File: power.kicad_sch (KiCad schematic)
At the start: 22 parts, among them U5 LM66100, U6 LM66100, U7 MAX77827AEFD+T, U8 SC4215

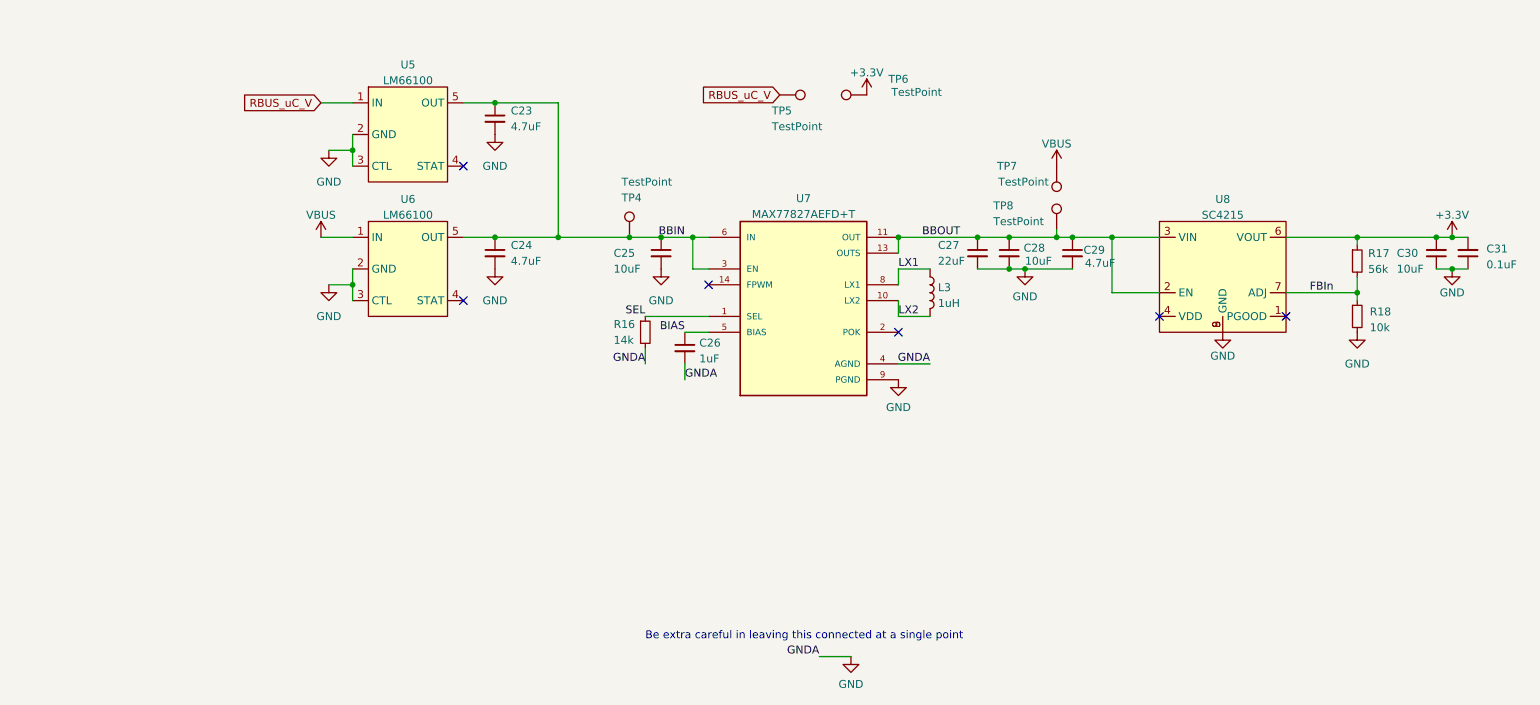
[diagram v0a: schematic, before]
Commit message: updated ideal oring diode and layout
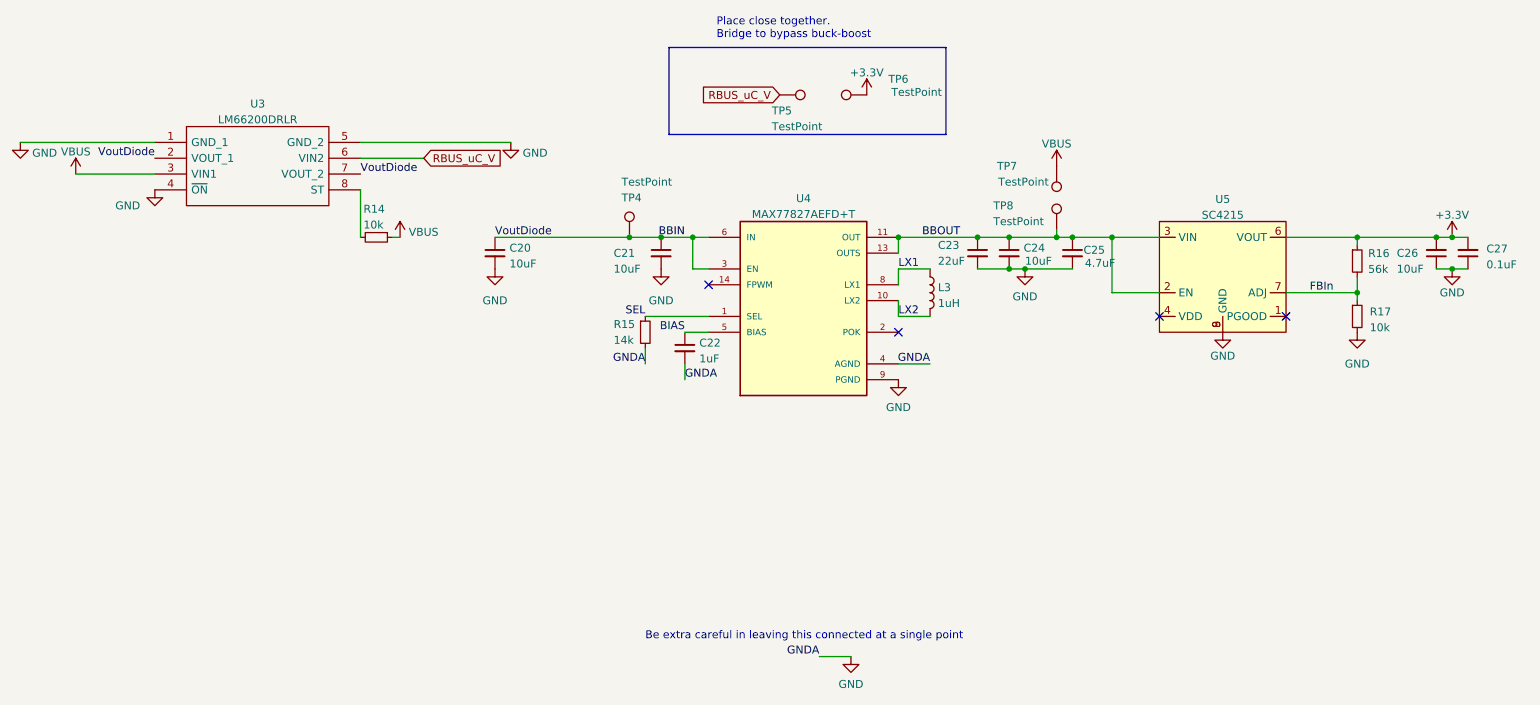
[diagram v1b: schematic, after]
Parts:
- removed C23: 4.7uF, Capacitor_SMD:C_0402_1005Metric, symbol Device:C_Small
- removed U5, U6: LM66100, Package_TO_SOT_SMD:SOT-23-5, symbol iclr:LTC4411
- added R14: 10k, Resistor_SMD:R_0402_1005Metric, symbol Device:R_Small
- added U3: LM66200DRLR, SOTFL50P160X60-8N, symbol iclr:LM66200DRLR
- C20: renamed from C24; value 4.7uF -> 10uF
- renumbered C25 to C21, C26 to C22, C27 to C23, C28 to C24, C29 to C25, C30 to C26, C31 to C27, R16 to R15, R17 to R16, R18 to R17, U7 to U4, U8 to U5
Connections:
- net BBIN: now also U3.2 (VOUT_1), U3.7 (VOUT_2)
- net GND: now also U3.1 (GND_1), U3.4 (~{ON}), U3.5 (GND_2)
- net RBUS_uC_V: now also U3.6 (VIN2)
- net VBUS: now also R14.1, U3.3 (VIN1)
- new net: R14.2, U3.8 (ST)
- no-connect marks 6 -> 4
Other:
- note added: "Place close together. Bridge to bypass buck-boost"

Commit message: changed usb port footprint to the combined SMD/THT one
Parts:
- U3: footprint SOTFL50P160X60-8N -> iclr:SOTFL50P160X60-8N
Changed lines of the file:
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@@
     (property "Reference" "U3" (id 0) (at 63.5 30.641 0))
     (property "Value" "LM66200DRLR" (id 1) (at 63.5 33.1779 0))
-    (property "Footprint" "SOTFL50P160X60-8N" (id 2) (at 76.2 34.29 0)
+    (property "Footprint" "iclr:SOTFL50P160X60-8N" (id 2) (at 76.2 34.29 0)
       (effects (font (size 1.27 1.27)) (justify left) hide)
     )

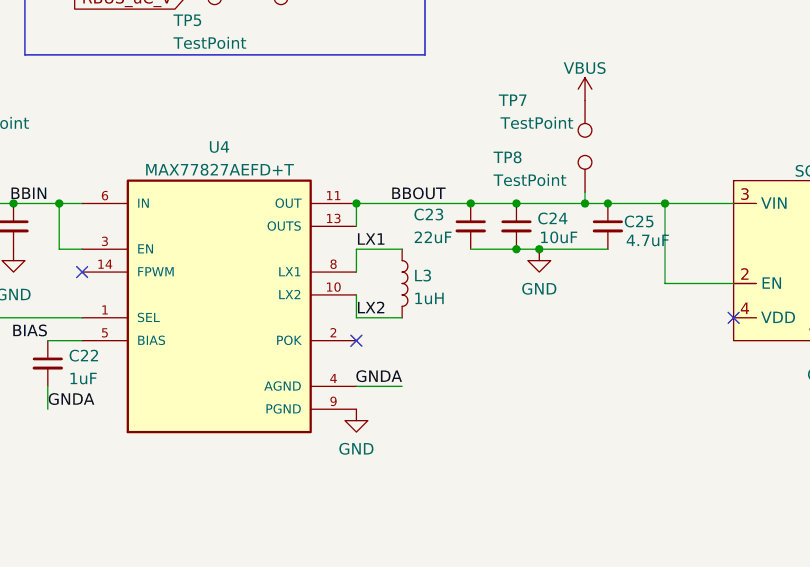
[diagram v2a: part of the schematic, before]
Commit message: updated some schematic values
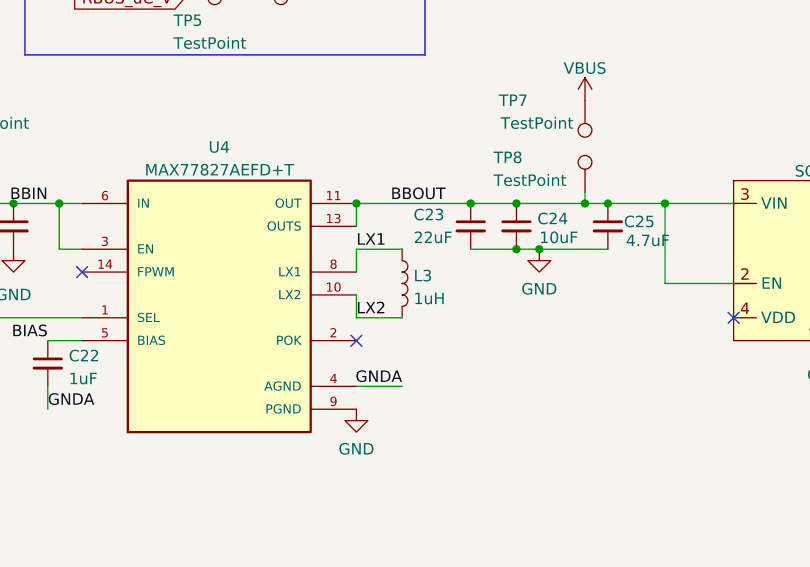
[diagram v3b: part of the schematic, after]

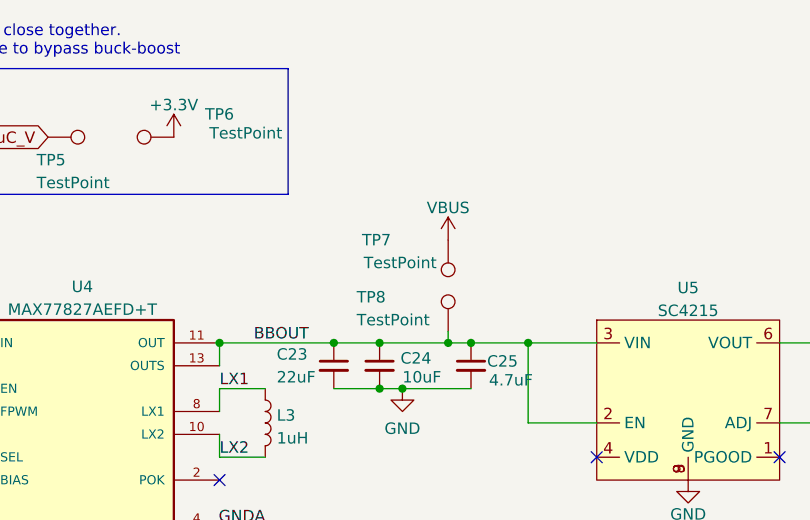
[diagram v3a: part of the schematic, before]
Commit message: implemented fixes that were changed for ordering of nimbus flight electronics, tidied up layout and set up manufacturing constraints
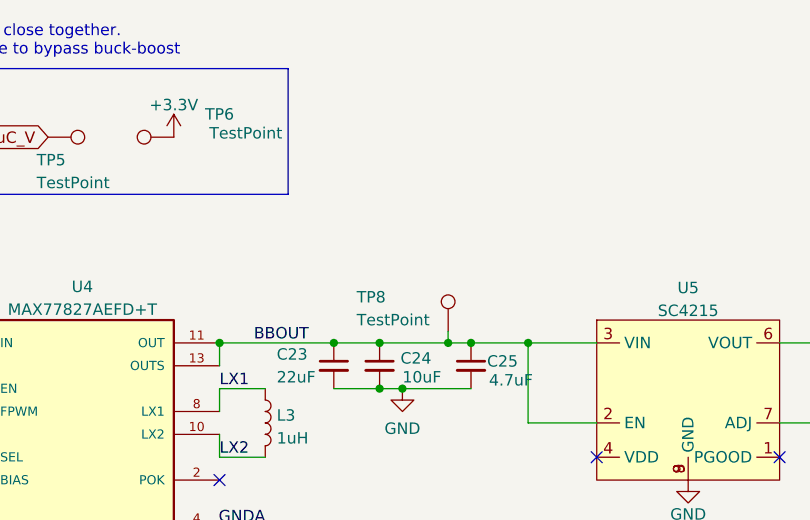
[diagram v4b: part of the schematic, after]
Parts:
- removed TP7: TestPoint, TestPoint:TestPoint_Pad_D1.5mm, symbol Connector:TestPoint
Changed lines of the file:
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@@
-    )
-  )
-  (symbol (lib_id "power:VBUS") (at 191.77 40.64 0) (unit 1)
-    (in_bom yes) (on_board yes) (dnp no) (fields_autoplaced)
-    (property "Reference" "#PWR046" (at 191.77 44.45 0)
-      (effects (font (size 1.27 1.27)) hide)
-    )
-    (property "Value" "VBUS" (at 191.77 37.0642 0)
-      (effects (font (size 1.27 1.27)))
-    )
-    (property "Footprint" "" (at 191.77 40.64 0)
-      (effects (font (size 1.27 1.27)) hide)
-    )
-    (property "Datasheet" "" (at 191.77 40.64 0)
-      (effects (font (size 1.27 1.27)) hide)
-    )
-    (pin "1")
-    (instances
-      (project "RicardoTemplate"
-        (path "/7db990e4-92e1-4f99-b4d2-435bbec1ba83/48a413b4-b7c2-44ac-971c-583c31b73475"
-          (reference "#PWR046") (unit 1)
-        )
-      )
     )
   )
@@
         )
       )
-    )
-  )
-  (symbol (lib_id "Connector:TestPoint") (at 191.77 40.64 180) (unit 1)
-    (in_bom yes) (on_board yes) (dnp no)
-    (property "Reference" "TP7" (at 185.42 40.64 0)
-      (effects (font (size 1.27 1.27)) (justify left))
-    )
-    (property "Value" "TestPoint" (at 190.5 43.1769 0)
-      (effects (font (size 1.27 1.27)) (justify left))
-    )
-    (property "Footprint" "TestPoint:TestPoint_Pad_D1.5mm" (at 186.69 40.64 0)
-      (effects (font (size 1.27 1.27)) hide)
-    )
-    (property "Datasheet" "~" (at 186.69 40.64 0)
-      (effects (font (size 1.27 1.27)) hide)
-    )
-    (pin "1")
-    (instances
-      (project "RicardoTemplate"
-        (path "/7db990e4-92e1-4f99-b4d2-435bbec1ba83/48a413b4-b7c2-44ac-971c-583c31b73475"
-          (reference "TP7") (unit 1)
-        )
-      )

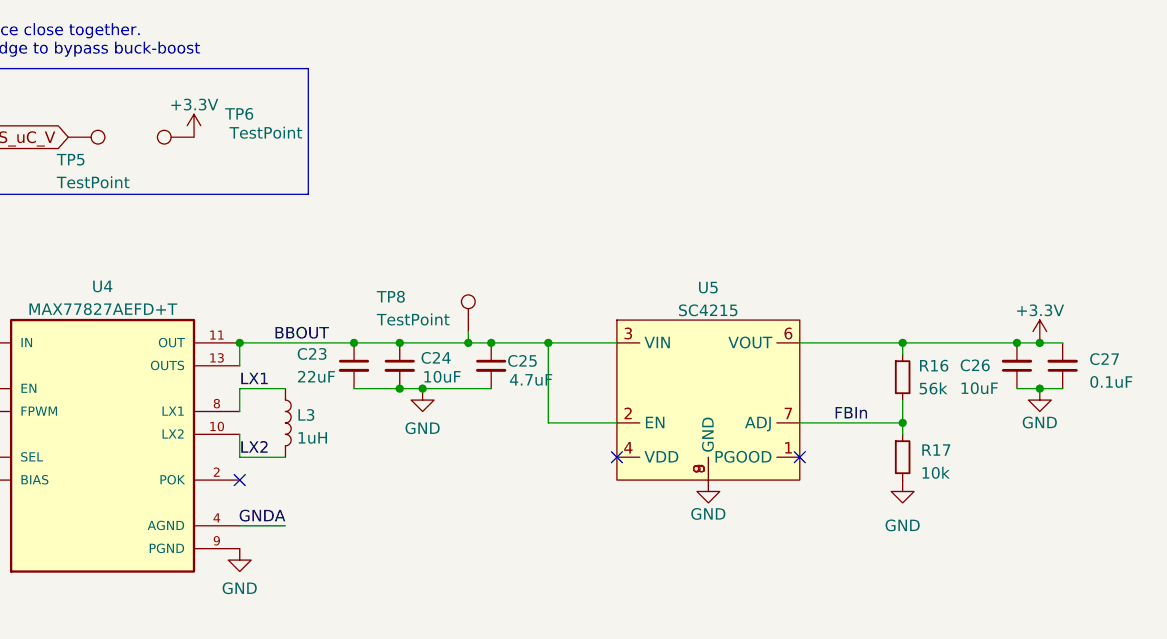
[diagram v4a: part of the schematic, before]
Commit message: Added CAN LEDs and some general fixes noticed over the year
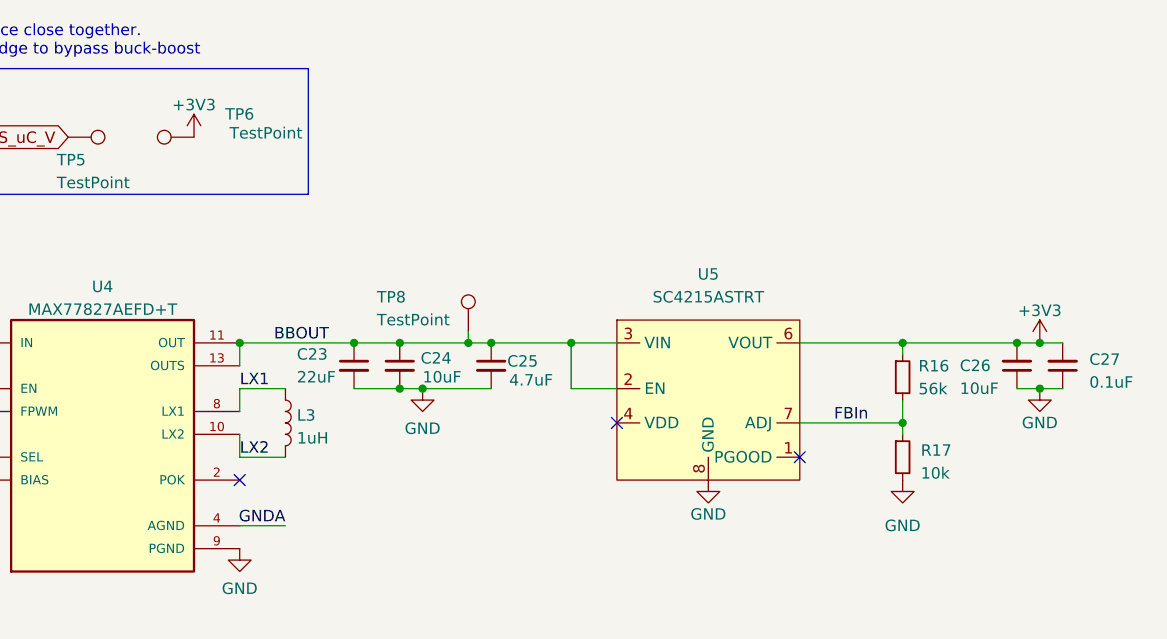
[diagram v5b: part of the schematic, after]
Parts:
- U5: value SC4215 -> SC4215ASTRT; symbol iclr:RT9025-25GSP -> iclr:SC4215ASTRT
